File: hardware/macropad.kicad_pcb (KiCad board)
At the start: 2 copper layers, 21 parts, among them J1 Conn_01x04, J2 Conn_01x06, SW1 SW_Push, SW10 RotaryEncoder_Switch, SW2 SW_Push, SW3 SW_Push, SW4 SW_Push, SW5 SW_Push, SW6 SW_Push, SW7 SW_Push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

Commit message: :sparkles: Add pico & screen
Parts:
- removed SW10: RotaryEncoder_Switch, 4ms_Encoder:ENC_SPST_12mm
- added J3: Screen connector, Connector_PinHeader_2.54mm:PinHeader_1x04_P2.54mm_Vertical, F.Cu at (83.8, 30.5)
- added U1: Pico, MCU_RaspberryPi_and_Boards:RPi_Pico_SMD_TH, F.Cu at (92.7, 49.5)
- J1: value Conn_01x04 -> Screen
- J2: footprint Connector_PinHeader_2.54mm:PinHeader_1x06_P2.54mm_Horizontal -> Connector_PinHeader_2.54mm:PinHeader_1x06_P2.54mm_Vertical
- moved J1 26.7 mm to (87.6, -5.08)
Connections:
- J1 pad 1: VDD -> 3V3
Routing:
- net ROW3: track 131.4 -> 138.4 mm
- net ROW2: track 114.3 -> 121.3 mm
- net ROW1: track 62.3 -> 68.7 mm
- net COL3: track 81.2 -> 87.6 mm
- net COL2: track 79.2 -> 85.6 mm
- net COL1: track 92.5 -> 98.9 mm

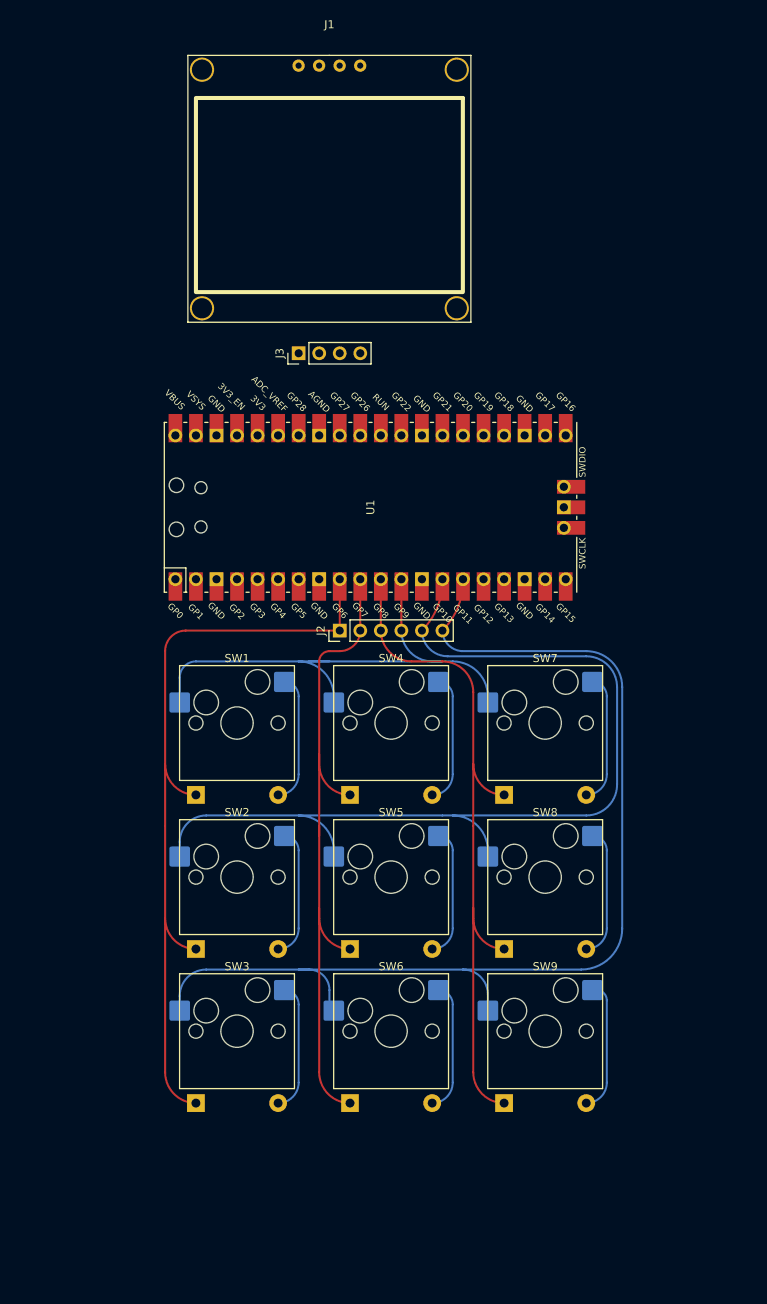
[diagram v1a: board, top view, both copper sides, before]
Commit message: :construction: Add headers for SPI screen also
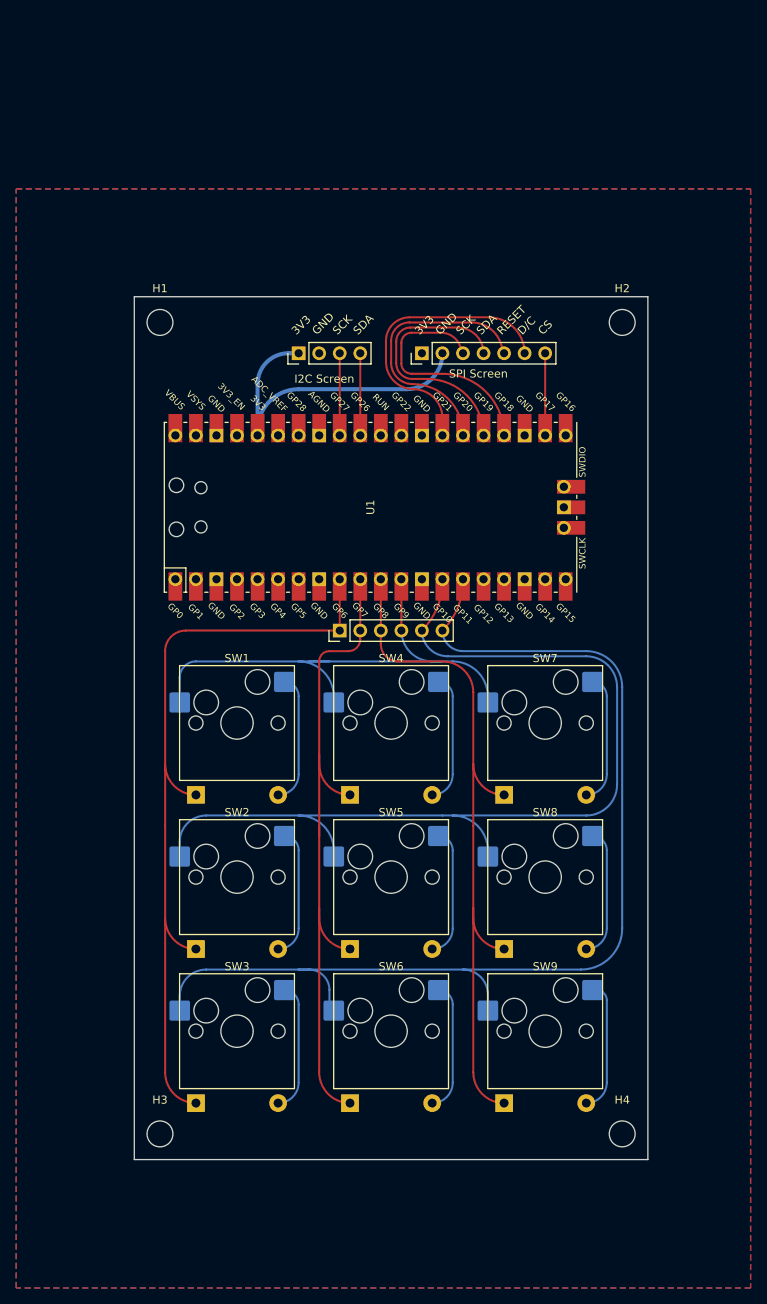
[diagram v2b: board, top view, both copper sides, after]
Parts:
- removed J1: Screen, nn_lib:I2C_1.3inch_OLED
- added H1: MountingHole, MountingHole:MountingHole_3.2mm_M3, F.Cu at (66.7, 26.7)
- added H2: MountingHole, MountingHole:MountingHole_3.2mm_M3, F.Cu at (123.8, 26.7)
- added H3: MountingHole, MountingHole:MountingHole_3.2mm_M3, F.Cu at (66.7, 127.0)
- added H4: MountingHole, MountingHole:MountingHole_3.2mm_M3, F.Cu at (123.8, 127.0)
- added J4: SPI Screen, Connector_PinHeader_2.54mm:PinHeader_1x07_P2.54mm_Vertical, F.Cu at (99.1, 30.5)
- J3: value Screen connector -> I2C Screen
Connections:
- U1 pad 22: unconnected-(U1-Pad22) -> SPI0_CS
- U1 pad 24: unconnected-(U1-Pad24) -> SPI0_SCK
- U1 pad 25: unconnected-(U1-Pad25) -> SPI0_TX
- U1 pad 26: unconnected-(U1-Pad26) -> SCREEN_RESET
- U1 pad 27: unconnected-(U1-Pad27) -> SCREEN_COMMAND
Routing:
- net 3V3: track 0.00 -> 42.0 mm
- net SCREEN_COMMAND: track 0.00 -> 36.4 mm
- net SCREEN_RESET: track 0.00 -> 33.6 mm
- net SPI0_TX: track 0.00 -> 31.6 mm
- net SPI0_SCK: track 0.00 -> 29.6 mm
- net SPI0_CS: track 0.00 -> 10.2 mm
- net SDA: track 0.00 -> 10.2 mm
- net SCK: track 0.00 -> 10.2 mm
- net COL3: track 87.6 -> 88.4 mm
- net COL2: track 85.6 -> 86.1 mm
- added copper zone on B.Cu, net GND
- added copper zone on F.Cu, net GND
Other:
- board outline added: 63.5 x 106.7 mm
- board text added: "3V3"
- board text added: "CS"
- board text added: "D/C"
- board text added: "GND"
- board text added: "RESET"
- board text added: "SCK"
- board text added: "SDA"
